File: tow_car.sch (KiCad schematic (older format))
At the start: 35 parts, among them J1 Conn_01x04_Male, J10 Conn_01x04_Male, J11 Conn_01x01_Male, J12 Conn_01x01, J13 Conn_01x02_Male, J14 Conn_01x01_Male, J15 Conn_01x03, J16 Conn_01x04_Male, J17 Conn_01x04_Male, J2 Conn_01x04_Male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

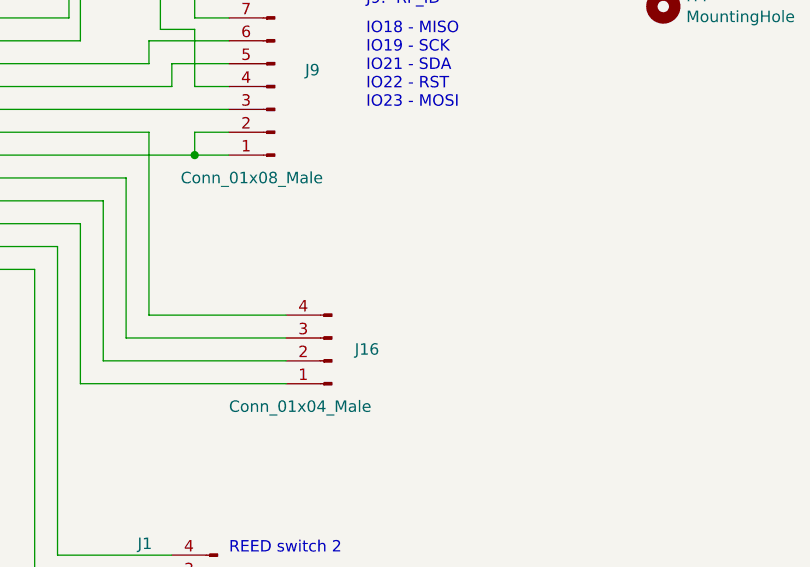
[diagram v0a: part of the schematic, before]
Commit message: Update comment for J16
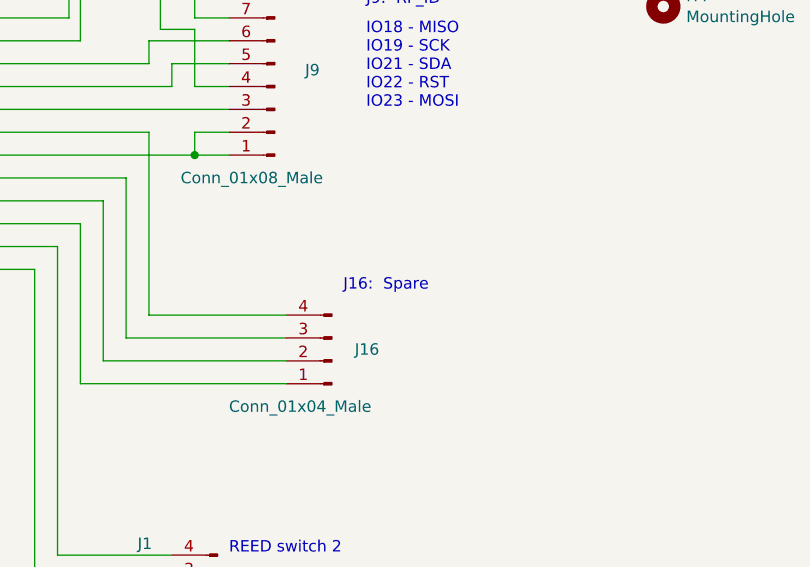
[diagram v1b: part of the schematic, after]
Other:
- note added: "J16: Spare"
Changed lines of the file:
@@
 Text Notes 700  5000 0    50   ~ 0
 External 5V
+Text Notes 8700 3100 0    50   ~ 0
+J16:  Spare
 $EndSCHEMATC

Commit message: Misc updates
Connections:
- net at U2.6 (OUT1): now also J17.1 (Pin_1); no longer J17.4 (Pin_4)
- net at U2.8 (OUT2): now also J17.4 (Pin_4); no longer J17.3 (Pin_3)
- net at J13.1 (Pin_1): now also J17.3 (Pin_3); no longer J17.1 (Pin_1)
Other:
- note added: "Pin 3: Power supply +9.0V"
- note added: "Power supply switch ON/OFF"
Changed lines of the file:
@@
 	3400 1450 4500 1450
-Wire Wire Line
-	1650 1950 2500 1950
 Wire Wire Line
 	5400 2500 3850 2500
@@
 Connection ~ 2750 2900
 Wire Wire Line
-	1400 2050 1400 1950
-Wire Wire Line
-	1400 1950 1100 1950
-Wire Wire Line
-	1400 2050 2500 2050
-Wire Wire Line
-	1650 1950 1650 1850
-Wire Wire Line
-	1650 1850 1100 1850
-Wire Wire Line
 	1100 1750 1500 1750
 Wire Wire Line
@@
 	1    0    0    -1
 $EndComp
-Wire Wire Line
-	1050 2450 1600 2450
 Connection ~ 2350 2400
 Text Notes 700  2350 0    50   ~ 0
@@
 $EndComp
 Wire Wire Line
-	1100 1650 1600 1650
-Wire Wire Line
 	2100 2250 2100 2400
 Wire Wire Line
 	2100 2400 2350 2400
-Wire Wire Line
-	1600 1650 1600 2450
 Wire Wire Line
 	1050 2550 1900 2550
@@
 Text Notes 8700 3100 0    50   ~ 0
 J16:  Spare
+Wire Wire Line
+	1100 1650 1900 1650
+Wire Wire Line
+	1050 2450 1250 2450
+Wire Wire Line
+	1250 2450 1250 1850
+Wire Wire Line
+	1250 1850 1100 1850
+Wire Wire Line
+	2500 2050 1900 2050
+Wire Wire Line
+	1900 1650 1900 2050
+Wire Wire Line
+	1100 1950 2500 1950
+Text Notes 700  1450 0    50   ~ 0
+Pin 3: Power supply +9.0V
+Text Notes 600  2750 0    50   ~ 0
+Power supply switch ON/OFF
 $EndSCHEMATC

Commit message: Mupp
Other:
- note added: "3.3V"
- note added: "GND"
- note added: "MISO"
- note added: "MOSI"
- note added: "RST"
- note added: "SCK"
- note added: "SDA"
- note removed: "IO18 - MISO\nIO19 - SCK\nIO21 - SDA\nIO22 - RST\nIO23 - MOSI"
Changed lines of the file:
@@
 Text Notes 2850 6300 0    50   ~ 0
 HC-SR04
-Text Notes 8800 1850 0    50   ~ 0
+Text Notes 8750 2100 0    50   ~ 0
 J9:  RF_ID
 Text Notes 4050 1450 0    50   ~ 0
@@
 Wire Wire Line
 	1900 3950 2150 3950
-Text Notes 8800 2300 0    50   ~ 0
-IO18 - MISO\nIO19 - SCK\nIO21 - SDA\nIO22 - RST\nIO23 - MOSI
 Wire Wire Line
 	6650 2000 7550 2000
@@
 U 1 1 5FD7A0AE
 P 8400 2200
-F 0 "J9" H 8235 2128 50  0000 C CNN
+F 0 "J9" H 8450 1700 50  0000 C CNN
 F 1 "Conn_01x08_Male" H 8500 2600 50  0000 C CNN
 F 2 "Connector_Molex:Molex_Micro-Fit_3.0_43045-0800_2x04_P3.00mm_Horizontal" H 8400 2200 50  0001 C CNN
@@
 	3400 1150 3400 1250
 Connection ~ 3400 1250
-NoConn ~ 3550 2350
+NoConn ~ 2900 1900
 $Comp
 L Device:CP C5
@@
 Text Notes 600  2750 0    50   ~ 0
 Power supply switch ON/OFF
+Text Notes 8450 2300 0    50   ~ 0
+MISO
+Text Notes 8450 1800 0    50   ~ 0
+MOSI
+Text Notes 8450 2100 0    50   ~ 0
+SCK
+Text Notes 8450 2000 0    50   ~ 0
+SDA
+Text Notes 8450 1900 0    50   ~ 0
+RST
+Text Notes 8450 2200 0    50   ~ 0
+3.3V
+Text Notes 8450 2400 0    50   ~ 0
+GND
 $EndSCHEMATC

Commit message: Clean up
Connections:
- net GND: now also J2.1 (Pin_1); no longer J2.4 (Pin_4)
- net at J5.2 (Pin_2): now also J2.4 (Pin_4); no longer J2.1 (Pin_1)
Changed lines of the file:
@@
 Text Notes 2300 6050 0    50   ~ 0
 5V
-Wire Wire Line
-	1650 5050 1650 4650
-Connection ~ 2250 5350
 $Comp
 L Connector_Generic:Conn_01x03 J15
@@
 $EndComp
 Wire Wire Line
-	1300 5050 1650 5050
-Wire Wire Line
 	7500 5100 7500 4850
 Wire Wire Line
@@
 Wire Wire Line
 	7900 1250 7900 1950
-Wire Wire Line
-	1300 5350 2250 5350
 Wire Wire Line
 	3900 4950 3900 3700
@@
 Text Notes 8450 2400 0    50   ~ 0
 GND
+Wire Wire Line
+	1300 5050 1500 5050
+Wire Wire Line
+	1500 5050 1500 5200
+Wire Wire Line
+	1500 5200 1900 5200
+Wire Wire Line
+	1900 5200 1900 5350
+Wire Wire Line
+	1900 5350 2250 5350
+Connection ~ 2250 5350
+Wire Wire Line
+	1300 5350 1650 5350
+Wire Wire Line
+	1650 5350 1650 4650
 $EndSCHEMATC
